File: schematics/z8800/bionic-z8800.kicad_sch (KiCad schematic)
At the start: 5 parts, among them J1 Bionic-P135, J2 Bionic-P245, U1 Z88C00, U3 11AA010-I/TO

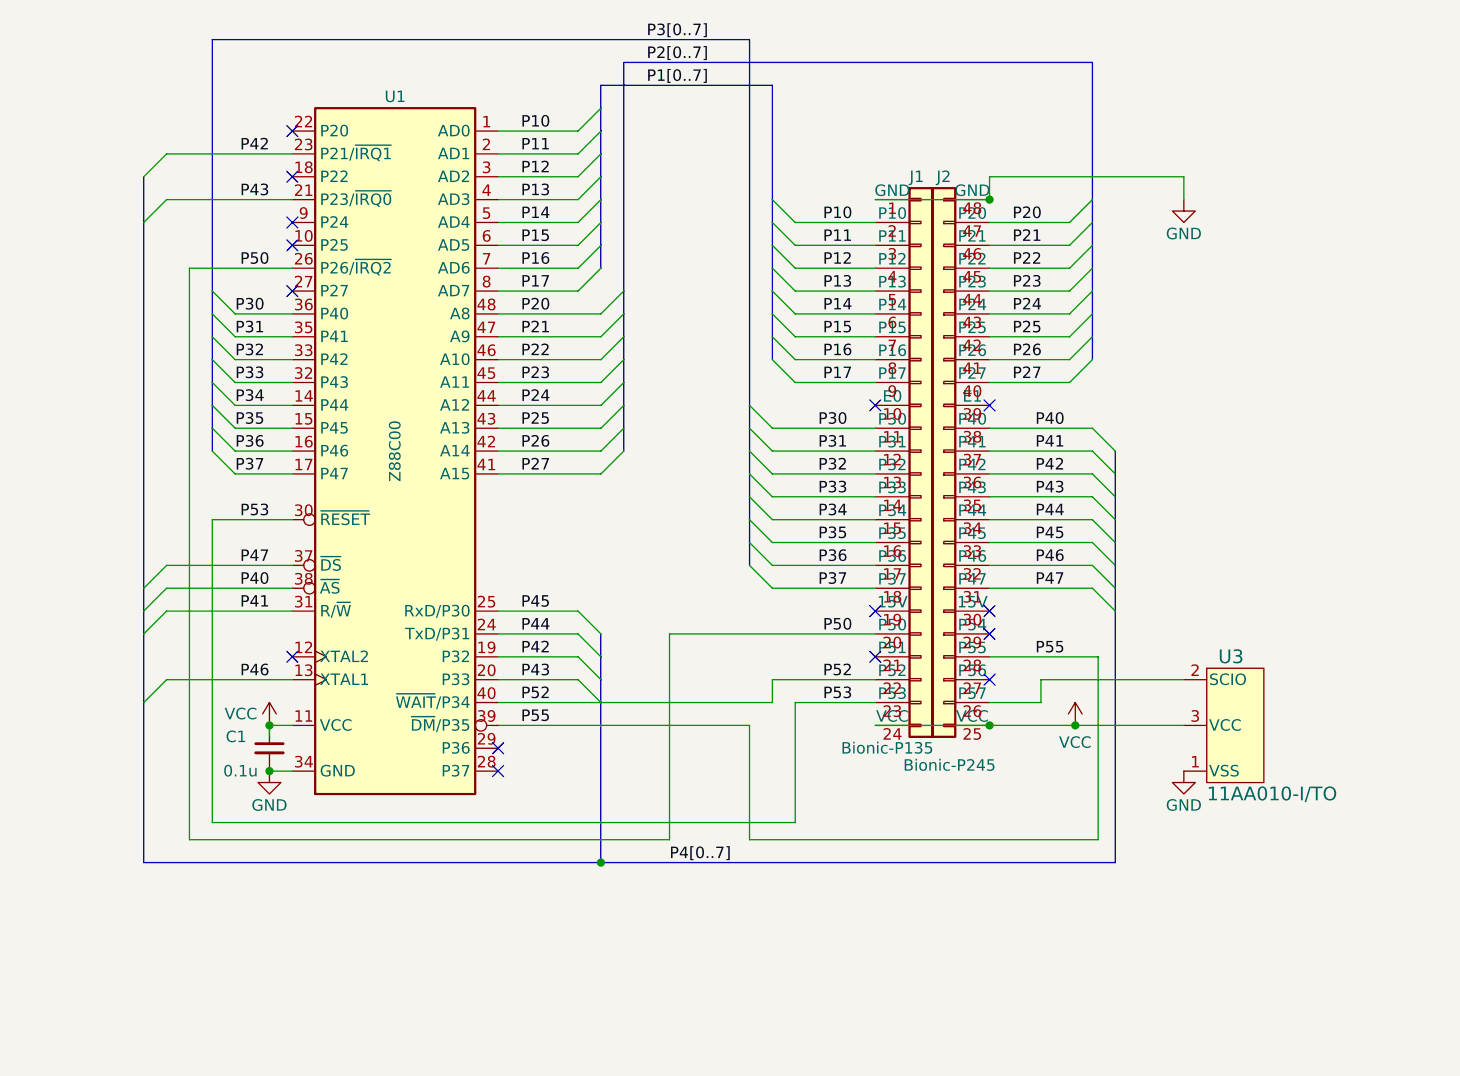
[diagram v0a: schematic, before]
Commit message: [Z8] Unify Z86 and Z88 debugger
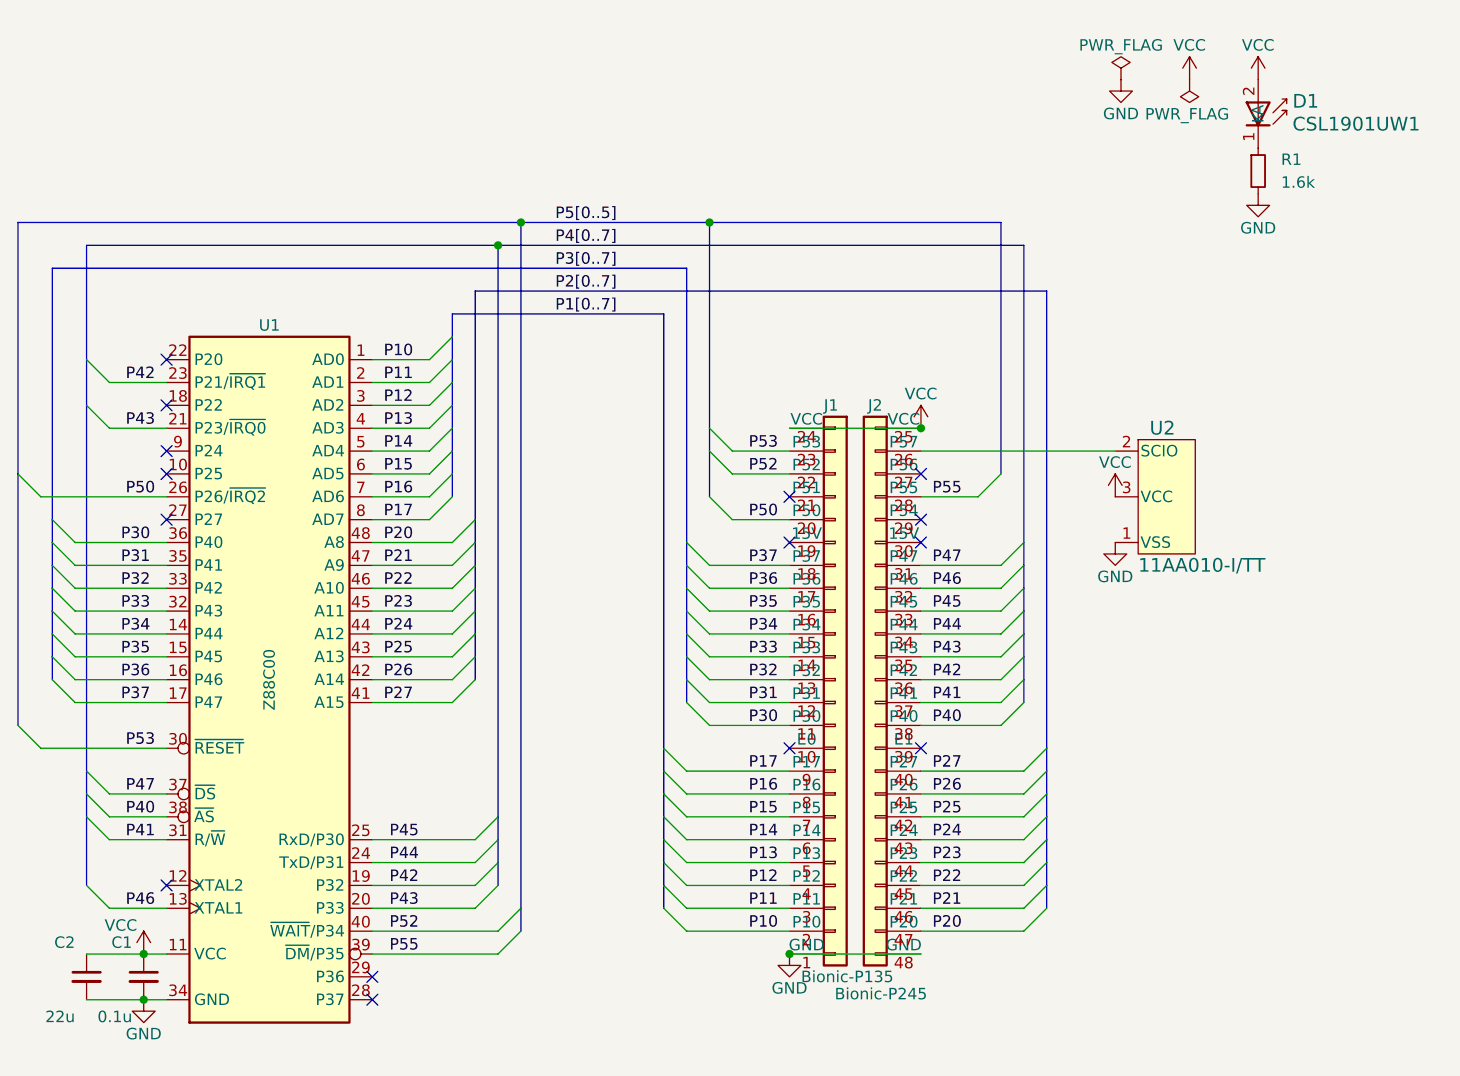
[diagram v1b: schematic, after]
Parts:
- removed U3: 11AA010-I/TO, TO-92_MC_MCH, symbol 0-LocalLibrary:11AA010-I_TO
- added C2: 22u, Capacitor_SMD:C_0603_1608Metric_Pad1.08x0.95mm_HandSolder, symbol Device:C_Small
- added D1: CSL1901UW1, 0-LocalLibrary:LED_CSL1901UW1_ROM, symbol 0-LocalLibrary:CSL1901UW1
- added R1: 1.6k, Resistor_SMD:R_0603_1608Metric_Pad0.98x0.95mm_HandSolder, symbol Device:R_Small
- added U2: 11AA010-I/TT, 0-LocalLibrary:SOT-23_MC_MCH-M, symbol 0-LocalLibrary:11AA010-I_TT
- C1: footprint Capacitor_THT:C_Disc_D3.4mm_W2.1mm_P2.50mm -> Capacitor_SMD:C_0603_1608Metric_Pad1.08x0.95mm_HandSolder
- J1: footprint connector:Bionic-P135_Vertical -> 0-LocalLibrary:Bionic-P135_Vertical
- J2: footprint connector:Bionic-P245_Vertical -> 0-LocalLibrary:Bionic-P245_Vertical
- U1: footprint Package_DIP:DIP-48_W15.24mm -> 0-LocalLibrary:DIP-48_W15.24mm_Socket
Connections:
- net GND: now also C2.2, R1.2, U2.1 (VSS)
- net VCC: now also C2.1, D1.2 (A), U2.3 (VCC)
- net at J2.26 (P57): now also U2.2 (SCIO)
- new net: D1.1 (K), R1.1
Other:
- moved on the sheet: C1, U1

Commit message: [schematics] Make board edges round
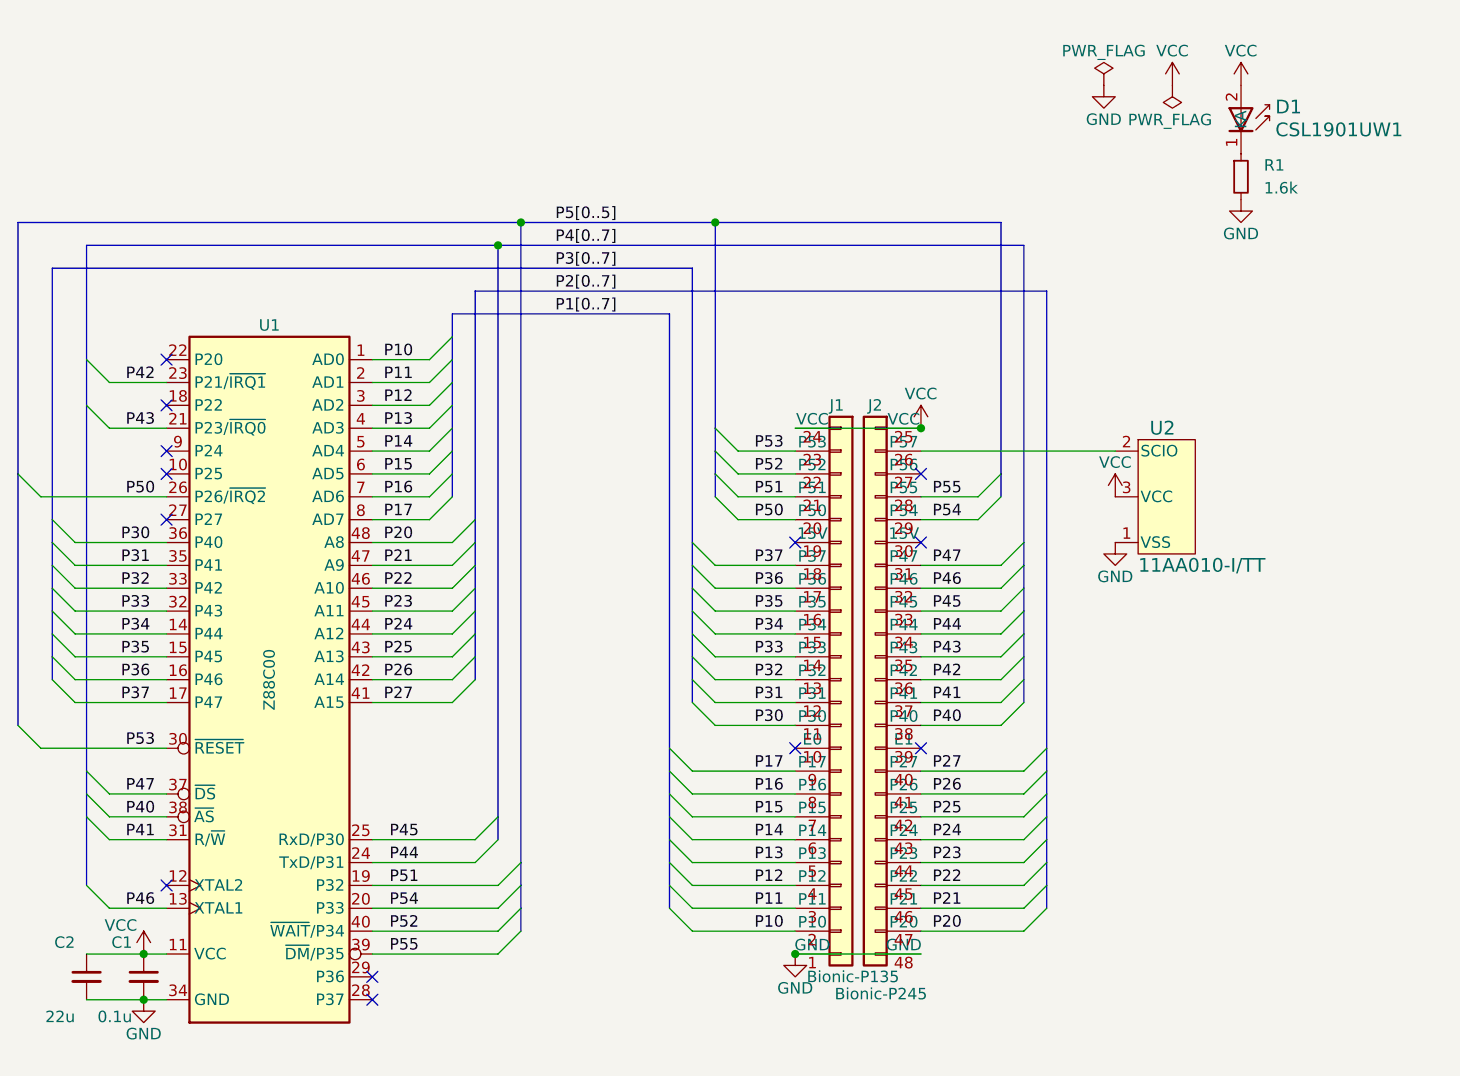
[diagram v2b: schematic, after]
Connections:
- net P42: no longer U1.19 (P32)
- net P43: no longer U1.20 (P33)
- net P54: now reaches J2.29 (P54)
- net P54: now also U1.20 (P33)
- net P51: now reaches J1.21 (P51)
- net P51: now also U1.19 (P32)
- no-connect marks 15 -> 13
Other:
- moved on the sheet: D1, J1, R1

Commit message: [Z8800] Fix EEPROM pinout
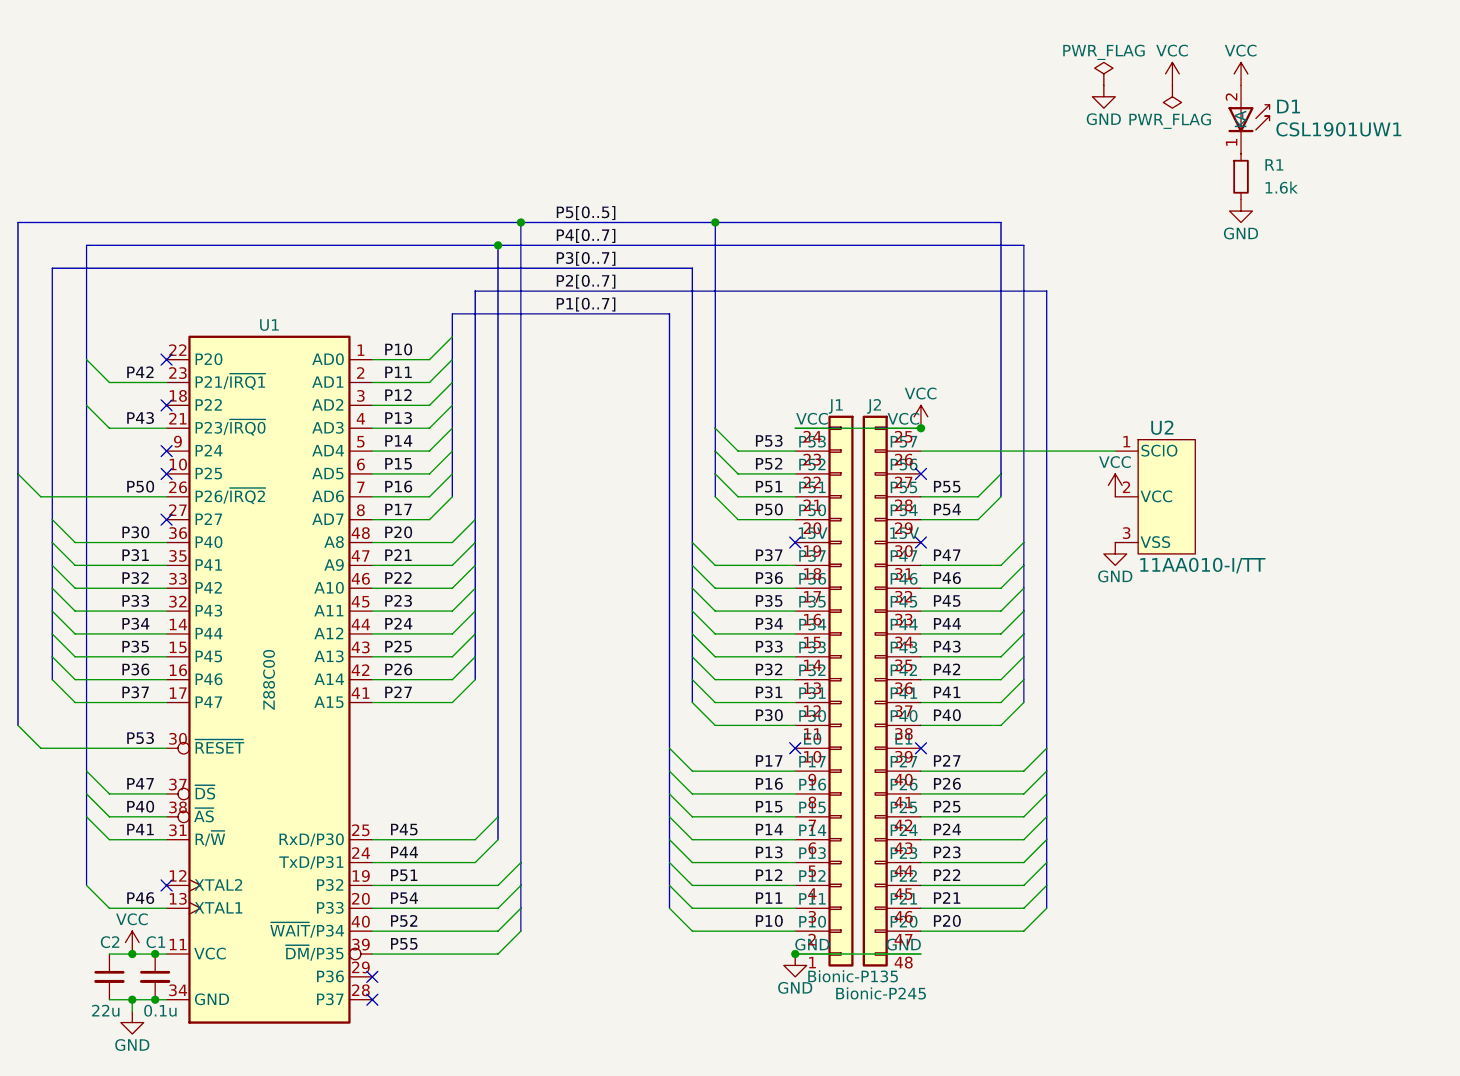
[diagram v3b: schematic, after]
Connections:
- net GND: now also U2.3 (VSS); no longer U2.1 (VSS)
- net VCC: now also U2.2 (VCC); no longer U2.3 (VCC)
- net at J2.26 (P57): now also U2.1 (SCIO); no longer U2.2 (SCIO)
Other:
- moved on the sheet: C1, C2
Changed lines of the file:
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@@
   (title_block
     (title "BionicZ8800")
-    (date "2024-10-24")
-    (rev "4")
+    (date "2024-11-02")
+    (rev "5")
     (company "Tadashi G. Takaoka")
   )
-  (junction (at 80.01 129.54) (diameter 0) (color 0 0 0 0)
+  (junction (at 78.74 134.62) (diameter 0) (color 0 0 0 0)
+  )
+  (junction (at 81.28 134.62) (diameter 0) (color 0 0 0 0)
   )
   (junction (at 119.38 50.8) (diameter 0) (color 0 0 0 0)
@@
   (junction (at 166.37 71.12) (diameter 0) (color 0 0 0 0)
   )
-  (junction (at 80.01 134.62) (diameter 0) (color 0 0 0 0)
-  )
   (junction (at 121.92 48.26) (diameter 0) (color 0 0 0 0)
   )
   (junction (at 143.51 48.26) (diameter 0) (color 0 0 0 0)
+  )
+  (junction (at 81.28 129.54) (diameter 0) (color 0 0 0 0)
+  )
+  (junction (at 78.74 129.54) (diameter 0) (color 0 0 0 0)
   )
   (junction (at 152.4 129.54) (diameter 0) (color 0 0 0 0)
@@
     (stroke (width 0) (type default))
   )
+  (wire (pts (xy 78.74 134.62) (xy 81.28 134.62))
+    (stroke (width 0) (type default))
+  )
   (wire (pts (xy 166.37 121.92) (xy 177.8 121.92))
     (stroke (width 0) (type default))
@@
     (stroke (width 0) (type default))
   )
-  (wire (pts (xy 73.66 129.54) (xy 80.01 129.54))
+  (wire (pts (xy 76.2 129.54) (xy 78.74 129.54))
     (stroke (width 0) (type default))
   )
@@
     (stroke (width 0) (type default))
   )
-  (wire (pts (xy 73.66 134.62) (xy 80.01 134.62))
+  (wire (pts (xy 76.2 134.62) (xy 78.74 134.62))
     (stroke (width 0) (type default))
   )
@@
     (stroke (width 0) (type default))
   )
+  (wire (pts (xy 78.74 129.54) (xy 81.28 129.54))
+    (stroke (width 0) (type default))
+  )
   (bus (pts (xy 121.92 124.46) (xy 121.92 127))
     (stroke (width 0) (type default))
@@
     (stroke (width 0) (type default))
   )
+  (wire (pts (xy 81.28 134.62) (xy 82.55 134.62))
+    (stroke (width 0) (type default))
+  )
   (wire (pts (xy 143.51 99.06) (xy 152.4 99.06))
     (stroke (width 0) (type default))
@@
     (stroke (width 0) (type default))
   )
+  (wire (pts (xy 81.28 129.54) (xy 82.55 129.54))
+    (stroke (width 0) (type default))
+  )
   (wire (pts (xy 76.2 111.76) (xy 82.55 111.76))
     (stroke (width 0) (type default))
@@
     (stroke (width 0) (type default))
   )
-  (wire (pts (xy 80.01 134.62) (xy 82.55 134.62))
-    (stroke (width 0) (type default))
-  )
   (wire (pts (xy 105.41 99.06) (xy 114.3 99.06))
     (stroke (width 0) (type default))
@@
     (stroke (width 0) (type default))
   )
-  (wire (pts (xy 80.01 129.54) (xy 82.55 129.54))
-    (stroke (width 0) (type default))
-  )
   (bus (pts (xy 138.43 114.3) (xy 138.43 116.84))
     (stroke (width 0) (type default))
@@
     (stroke (width 0) (type default))
   )
+  (wire (pts (xy 78.74 135.89) (xy 78.74 134.62))
+    (stroke (width 0) (type default))
+  )
   (bus (pts (xy 73.66 68.58) (xy 73.66 109.22))
     (stroke (width 0) (type default))
@@
     (effects (font (size 1.27 1.27)) (justify right bottom))
   )
-  (symbol (lib_id "Device:C_Small") (at 80.01 132.08 0) (mirror y) (unit 1)
-    (in_bom yes) (on_board yes) (dnp no)
-    (property "Reference" "C1" (at 78.74 128.27 0)
+  (symbol (lib_id "Device:C_Small") (at 81.28 132.08 0) (mirror y) (unit 1)
+    (in_bom yes) (on_board yes) (dnp no)
+    (property "Reference" "C1" (at 82.55 128.27 0)
       (effects (font (size 1.27 1.27)) (justify left))
     )
-    (property "Value" "0.1u" (at 78.74 136.525 0)
+    (property "Value" "0.1u" (at 83.82 135.89 0)
       (effects (font (size 1.27 1.27)) (justify left))
     )
-    (property "Footprint" "Capacitor_SMD:C_0603_1608Metric_Pad1.08x0.95mm_HandSolder" (at 80.01 132.08 0)
-      (effects (font (size 1.27 1.27)) hide)
-    )
-    (property "Datasheet" "~" (at 80.01 132.08 0)
+    (property "Footprint" "Capacitor_SMD:C_0603_1608Metric_Pad1.08x0.95mm_HandSolder" (at 81.28 132.08 0)
+      (effects (font (size 1.27 1.27)) hide)
+    )
+    (property "Datasheet" "~" (at 81.28 132.08 0)
       (effects (font (size 1.27 1.27)) hide)
     )
@@
     )
   )
-  (symbol (lib_id "power:GND") (at 80.01 134.62 0) (unit 1)
-    (in_bom yes) (on_board yes) (dnp no)
-    (property "Reference" "#PWR03" (at 80.01 140.97 0)
-      (effects (font (size 1.27 1.27)) hide)
-    )
-    (property "Value" "GND" (at 80.01 138.43 0)
+  (symbol (lib_id "power:GND") (at 78.74 135.89 0) (unit 1)
+    (in_bom yes) (on_board yes) (dnp no)
+    (property "Reference" "#PWR03" (at 78.74 142.24 0)
+      (effects (font (size 1.27 1.27)) hide)
+    )
+    (property "Value" "GND" (at 78.74 139.7 0)
       (effects (font (size 1.27 1.27)))
     )
-    (property "Footprint" "" (at 80.01 134.62 0)
-      (effects (font (size 1.27 1.27)) hide)
-    )
-    (property "Datasheet" "" (at 80.01 134.62 0)
+    (property "Footprint" "" (at 78.74 135.89 0)
+      (effects (font (size 1.27 1.27)) hide)
+    )
+    (property "Datasheet" "" (at 78.74 135.89 0)
       (effects (font (size 1.27 1.27)) hide)
     )
@@
     )
   )
-  (symbol (lib_id "Device:C_Small") (at 73.66 132.08 0) (mirror y) (unit 1)
-    (in_bom yes) (on_board yes) (dnp no)
-    (property "Reference" "C2" (at 72.39 128.27 0)
+  (symbol (lib_id "Device:C_Small") (at 76.2 132.08 0) (mirror y) (unit 1)
+    (in_bom yes) (on_board yes) (dnp no)
+    (property "Reference" "C2" (at 77.47 128.27 0)
       (effects (font (size 1.27 1.27)) (justify left))
     )
-    (property "Value" "22u" (at 72.39 136.525 0)
+    (property "Value" "22u" (at 77.47 135.89 0)
       (effects (font (size 1.27 1.27)) (justify left))
     )
-    (property "Footprint" "Capacitor_SMD:C_0603_1608Metric_Pad1.08x0.95mm_HandSolder" (at 73.66 132.08 0)
-      (effects (font (size 1.27 1.27)) hide)
-    )
-    (property "Datasheet" "~" (at 73.66 132.08 0)
+    (property "Footprint" "Capacitor_SMD:C_0603_1608Metric_Pad1.08x0.95mm_HandSolder" (at 76.2 132.08 0)
+      (effects (font (size 1.27 1.27)) hide)
+    )
+    (property "Datasheet" "~" (at 76.2 132.08 0)
       (effects (font (size 1.27 1.27)) hide)
     )
@@
     )
   )
-  (symbol (lib_id "power:VCC") (at 80.01 129.54 0) (unit 1)
-    (in_bom yes) (on_board yes) (dnp no)
-    (property "Reference" "#PWR07" (at 80.01 133.35 0)
-      (effects (font (size 1.27 1.27)) hide)
-    )
-    (property "Value" "VCC" (at 77.47 126.365 0)
+  (symbol (lib_id "power:VCC") (at 78.74 129.54 0) (unit 1)
+    (in_bom yes) (on_board yes) (dnp no)
+    (property "Reference" "#PWR07" (at 78.74 133.35 0)
+      (effects (font (size 1.27 1.27)) hide)
+    )
+    (property "Value" "VCC" (at 78.74 125.73 0)
       (effects (font (size 1.27 1.27)))
     )
-    (property "Footprint" "" (at 80.01 129.54 0)
-      (effects (font (size 1.27 1.27)) hide)
-    )
-    (property "Datasheet" "" (at 80.01 129.54 0)
-      (effects (font (size 1.27 1.27)) hide)
-    )
+    (property "Footprint" "" (at 78.74 129.54 0)
+      (effects (font (size 1.27 1.27)) hide)
+    )
+    (property "Datasheet" "" (at 78.74 129.54 0)
+      (effects (font (size 1.27 1.27)) hide)
+    )

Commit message: [schematics] Update LED footprint
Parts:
- D1: footprint 0-LocalLibrary:LED_CSL1901UW1_ROM -> 0-LocalLibrary:LED_CSL1901UW1_ROM-M
